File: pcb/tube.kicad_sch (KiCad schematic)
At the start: 79 parts, among them J1 Screw_Terminal_01x02, J10 LED_[5..8], J11 LED_[1..4], J2 Screw_Terminal_01x02, J3 Screw_Terminal_01x02, J4 Conn_01x04_Pin, J5 Conn_01x08_Pin, J6 Conn_01x05_Pin, U1 INA226, U10 74LS32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

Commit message: PCB: Use 0805
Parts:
- C1, C2, C3, C4, C5, C6, C7, C8: footprint Capacitor_SMD:C_0603_1608Metric -> Capacitor_SMD:C_0805_2012Metric
- R10, R11, R12, R13, R14, R15, R16, R17, R18, R19, R20, R21, R22, R23, R4, R5, R6, R7, R8, R9: footprint Resistor_SMD:R_0603_1608Metric -> Resistor_SMD:R_0805_2012Metric
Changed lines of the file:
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@@
       (effects (font (size 1.27 1.27)) (justify bottom))
     )
-    (property "Footprint" "Resistor_SMD:R_0603_1608Metric" (at 240.03 187.452 90)
+    (property "Footprint" "Resistor_SMD:R_0805_2012Metric" (at 240.03 187.452 90)
       (effects (font (size 1.27 1.27)) hide)
     )
@@
       (effects (font (size 1.27 1.27)) (justify right))
     )
-    (property "Footprint" "Resistor_SMD:R_0603_1608Metric" (at 61.468 101.6 90)
+    (property "Footprint" "Resistor_SMD:R_0805_2012Metric" (at 61.468 101.6 90)
       (effects (font (size 1.27 1.27)) hide)
     )
@@
       (effects (font (size 1.27 1.27)) (justify left))
     )
-    (property "Footprint" "Resistor_SMD:R_0603_1608Metric" (at 111.76 128.778 90)
+    (property "Footprint" "Resistor_SMD:R_0805_2012Metric" (at 111.76 128.778 90)
       (effects (font (size 1.27 1.27)) hide)
     )
@@
       (effects (font (size 1.27 1.27)) (justify left))
     )
-    (property "Footprint" "Resistor_SMD:R_0603_1608Metric" (at 199.898 198.12 90)
+    (property "Footprint" "Resistor_SMD:R_0805_2012Metric" (at 199.898 198.12 90)
       (effects (font (size 1.27 1.27)) hide)
     )
@@
       (effects (font (size 1.27 1.27)))
     )
-    (property "Footprint" "Capacitor_SMD:C_0603_1608Metric" (at 123.19 21.8948 0)
+    (property "Footprint" "Capacitor_SMD:C_0805_2012Metric" (at 123.19 21.8948 0)
       (effects (font (size 1.27 1.27)) hide)
     )
@@
       (effects (font (size 1.27 1.27)))
     )
-    (property "Footprint" "Capacitor_SMD:C_0603_1608Metric" (at 37.7952 242.57 0)
+    (property "Footprint" "Capacitor_SMD:C_0805_2012Metric" (at 37.7952 242.57 0)
       (effects (font (size 1.27 1.27)) hide)
     )
@@
       (effects (font (size 1.27 1.27)) (justify left))
     )
-    (property "Footprint" "Resistor_SMD:R_0603_1608Metric" (at 185.928 46.99 90)
+    (property "Footprint" "Resistor_SMD:R_0805_2012Metric" (at 185.928 46.99 90)
       (effects (font (size 1.27 1.27)) hide)
     )
@@
       (effects (font (size 1.27 1.27)))
     )
-    (property "Footprint" "Capacitor_SMD:C_0603_1608Metric" (at 124.46 159.7152 0)
+    (property "Footprint" "Capacitor_SMD:C_0805_2012Metric" (at 124.46 159.7152 0)
       (effects (font (size 1.27 1.27)) hide)
     )
@@
       (effects (font (size 1.27 1.27)) (justify left))
     )
-    (property "Footprint" "Resistor_SMD:R_0603_1608Metric" (at 111.76 131.318 90)
+    (property "Footprint" "Resistor_SMD:R_0805_2012Metric" (at 111.76 131.318 90)
       (effects (font (size 1.27 1.27)) hide)
     )
@@
       (effects (font (size 1.27 1.27)))
     )
-    (property "Footprint" "Capacitor_SMD:C_0603_1608Metric" (at 36.83 21.8948 0)
+    (property "Footprint" "Capacitor_SMD:C_0805_2012Metric" (at 36.83 21.8948 0)
       (effects (font (size 1.27 1.27)) hide)
     )
@@
       (effects (font (size 1.27 1.27)) (justify right))
     )
-    (property "Footprint" "Resistor_SMD:R_0603_1608Metric" (at 282.448 119.38 90)
+    (property "Footprint" "Resistor_SMD:R_0805_2012Metric" (at 282.448 119.38 90)
       (effects (font (size 1.27 1.27)) hide)
     )
@@
       (effects (font (size 1.27 1.27)) (justify left))
     )
-    (property "Footprint" "Resistor_SMD:R_0603_1608Metric" (at 111.76 138.938 90)
+    (property "Footprint" "Resistor_SMD:R_0805_2012Metric" (at 111.76 138.938 90)
       (effects (font (size 1.27 1.27)) hide)
     )
@@
       (effects (font (size 1.27 1.27)) (justify left))
     )
-    (property "Footprint" "Resistor_SMD:R_0603_1608Metric" (at 111.76 121.158 90)
+    (property "Footprint" "Resistor_SMD:R_0805_2012Metric" (at 111.76 121.158 90)
       (effects (font (size 1.27 1.27)) hide)
     )
@@
       (effects (font (size 1.27 1.27)))
     )
-    (property "Footprint" "Capacitor_SMD:C_0603_1608Metric" (at 80.01 21.8948 0)
+    (property "Footprint" "Capacitor_SMD:C_0805_2012Metric" (at 80.01 21.8948 0)
       (effects (font (size 1.27 1.27)) hide)
     )
@@
       (effects (font (size 1.27 1.27)) (justify left))
     )
-    (property "Footprint" "Resistor_SMD:R_0603_1608Metric" (at 111.76 123.698 90)
+    (property "Footprint" "Resistor_SMD:R_0805_2012Metric" (at 111.76 123.698 90)
       (effects (font (size 1.27 1.27)) hide)
     )
@@
       (effects (font (size 1.27 1.27)))
     )
-    (property "Footprint" "Capacitor_SMD:C_0603_1608Metric" (at 26.3652 242.57 0)
+    (property "Footprint" "Capacitor_SMD:C_0805_2012Metric" (at 26.3652 242.57 0)
       (effects (font (size 1.27 1.27)) hide)
     )
@@
       (effects (font (size 1.27 1.27)) (justify bottom))
     )
-    (property "Footprint" "Resistor_SMD:R_0603_1608Metric" (at 220.98 176.022 90)
+    (property "Footprint" "Resistor_SMD:R_0805_2012Metric" (at 220.98 176.022 90)
       (effects (font (size 1.27 1.27)) hide)
     )
@@
       (effects (font (size 1.27 1.27)) (justify right))
     )
-    (property "Footprint" "Resistor_SMD:R_0603_1608Metric" (at 52.578 101.6 90)
+    (property "Footprint" "Resistor_SMD:R_0805_2012Metric" (at 52.578 101.6 90)
       (effects (font (size 1.27 1.27)) hide)
     )
@@
       (effects (font (size 1.27 1.27)) (justify left))
     )
-    (property "Footprint" "Resistor_SMD:R_0603_1608Metric" (at 111.76 133.858 90)
+    (property "Footprint" "Resistor_SMD:R_0805_2012Metric" (at 111.76 133.858 90)
       (effects (font (size 1.27 1.27)) hide)
     )
@@
       (effects (font (size 1.27 1.27)) (justify right))
     )
-    (property "Footprint" "Resistor_SMD:R_0603_1608Metric" (at 43.688 101.6 90)
+    (property "Footprint" "Resistor_SMD:R_0805_2012Metric" (at 43.688 101.6 90)
       (effects (font (size 1.27 1.27)) hide)
     )
@@
       (effects (font (size 1.27 1.27)) (justify left))
     )
-    (property "Footprint" "Resistor_SMD:R_0603_1608Metric" (at 111.76 136.398 90)
+    (property "Footprint" "Resistor_SMD:R_0805_2012Metric" (at 111.76 136.398 90)
       (effects (font (size 1.27 1.27)) hide)
     )
@@
       (effects (font (size 1.27 1.27)) (justify bottom))
     )
-    (property "Footprint" "Resistor_SMD:R_0603_1608Metric" (at 214.63 187.452 90)
+    (property "Footprint" "Resistor_SMD:R_0805_2012Metric" (at 214.63 187.452 90)
       (effects (font (size 1.27 1.27)) hide)
     )
@@
       (effects (font (size 1.27 1.27)) (justify bottom))
     )
-    (property "Footprint" "Resistor_SMD:R_0603_1608Metric" (at 234.95 176.022 90)
+    (property "Footprint" "Resistor_SMD:R_0805_2012Metric" (at 234.95 176.022 90)
       (effects (font (size 1.27 1.27)) hide)
     )
@@
       (effects (font (size 1.27 1.27)))
     )
-    (property "Footprint" "Capacitor_SMD:C_0603_1608Metric" (at 290.5252 64.77 0)
+    (property "Footprint" "Capacitor_SMD:C_0805_2012Metric" (at 290.5252 64.77 0)
       (effects (font (size 1.27 1.27)) hide)
     )
@@
       (effects (font (size 1.27 1.27)))
     )
-    (property "Footprint" "Capacitor_SMD:C_0603_1608Metric" (at 277.8252 64.77 0)
+    (property "Footprint" "Capacitor_SMD:C_0805_2012Metric" (at 277.8252 64.77 0)
       (effects (font (size 1.27 1.27)) hide)
     )
@@
       (effects (font (size 1.27 1.27)) (justify left))
     )
-    (property "Footprint" "Resistor_SMD:R_0603_1608Metric" (at 174.498 46.99 90)
+    (property "Footprint" "Resistor_SMD:R_0805_2012Metric" (at 174.498 46.99 90)
       (effects (font (size 1.27 1.27)) hide)
     )
@@
       (effects (font (size 1.27 1.27)) (justify left))
     )
-    (property "Footprint" "Resistor_SMD:R_0603_1608Metric" (at 111.76 126.238 90)
+    (property "Footprint" "Resistor_SMD:R_0805_2012Metric" (at 111.76 126.238 90)
       (effects (font (size 1.27 1.27)) hide)
     )
@@
       (effects (font (size 1.27 1.27)) (justify right))
     )
-    (property "Footprint" "Resistor_SMD:R_0603_1608Metric" (at 276.098 106.68 90)
+    (property "Footprint" "Resistor_SMD:R_0805_2012Metric" (at 276.098 106.68 90)
       (effects (font (size 1.27 1.27)) hide)
     )

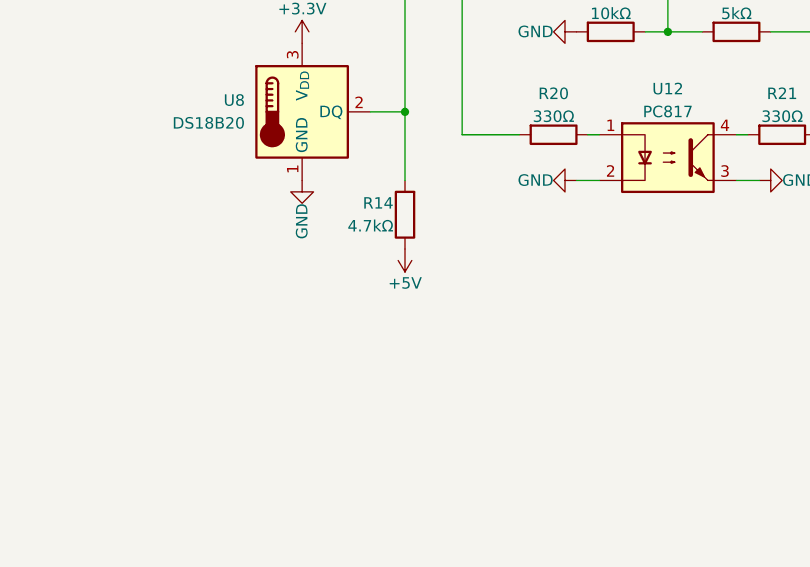
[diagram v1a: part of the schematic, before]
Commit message: PCB: Verify Pullups
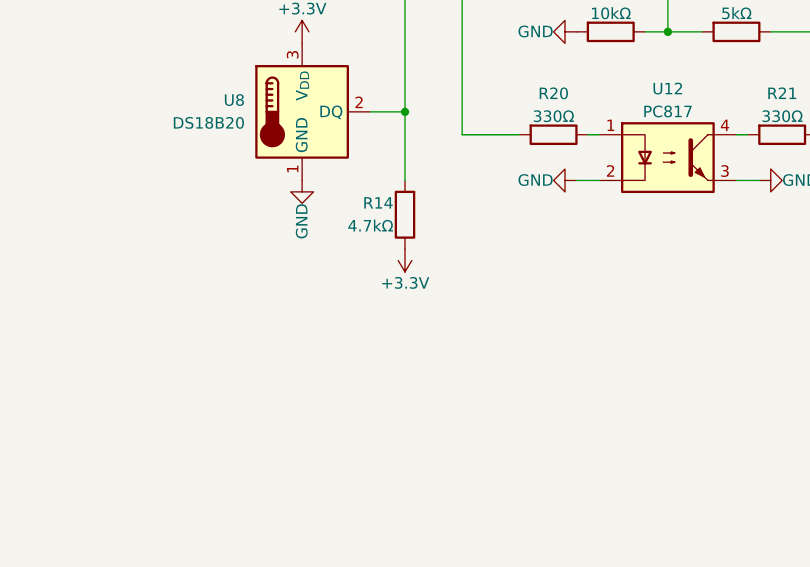
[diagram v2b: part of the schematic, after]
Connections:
- net +3.3V: now also R14.1
- net +5V: no longer R14.1
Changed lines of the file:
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@@
     )
   )
-  (symbol (lib_id "power:+5V") (at 198.12 201.93 180) (unit 1)
-    (in_bom yes) (on_board yes) (dnp no)
-    (property "Reference" "#PWR040" (at 198.12 198.12 0)
-      (effects (font (size 1.27 1.27)) hide)
-    )
-    (property "Value" "+5V" (at 198.12 205.74 0)
-      (effects (font (size 1.27 1.27)))
-    )
-    (property "Footprint" "" (at 198.12 201.93 0)
-      (effects (font (size 1.27 1.27)) hide)
-    )
-    (property "Datasheet" "" (at 198.12 201.93 0)
-      (effects (font (size 1.27 1.27)) hide)
-    )
-    (pin "1")
-    (instances
-      (project "tube"
-        (path "/17a681e7-f555-4501-b0f6-333651e2bfd6"
-          (reference "#PWR040") (unit 1)
-        )
-      )
-    )
-  )
   (symbol (lib_id "Connector:RJ45_Shielded") (at 67.31 173.99 0) (unit 1)
     (in_bom yes) (on_board yes) (dnp no)
@@
         )
       )
+    )
+  )
+  (symbol (lib_id "power:+3.3V") (at 198.12 201.93 180) (unit 1)
+    (in_bom yes) (on_board yes) (dnp no)
+    (property "Reference" "#PWR040" (at 198.12 198.12 0)
+      (effects (font (size 1.27 1.27)) hide)
+    )
+    (property "Value" "+3.3V" (at 198.12 205.74 0)
+      (effects (font (size 1.27 1.27)))
+    )
+    (property "Footprint" "" (at 198.12 201.93 0)
+      (effects (font (size 1.27 1.27)) hide)
+    )
+    (property "Datasheet" "" (at 198.12 201.93 0)
+      (effects (font (size 1.27 1.27)) hide)
+    )
+    (pin "1")
+    (instances
+      (project "tube"
+        (path "/17a681e7-f555-4501-b0f6-333651e2bfd6"
+          (reference "#PWR040") (unit 1)
+        )
+      )

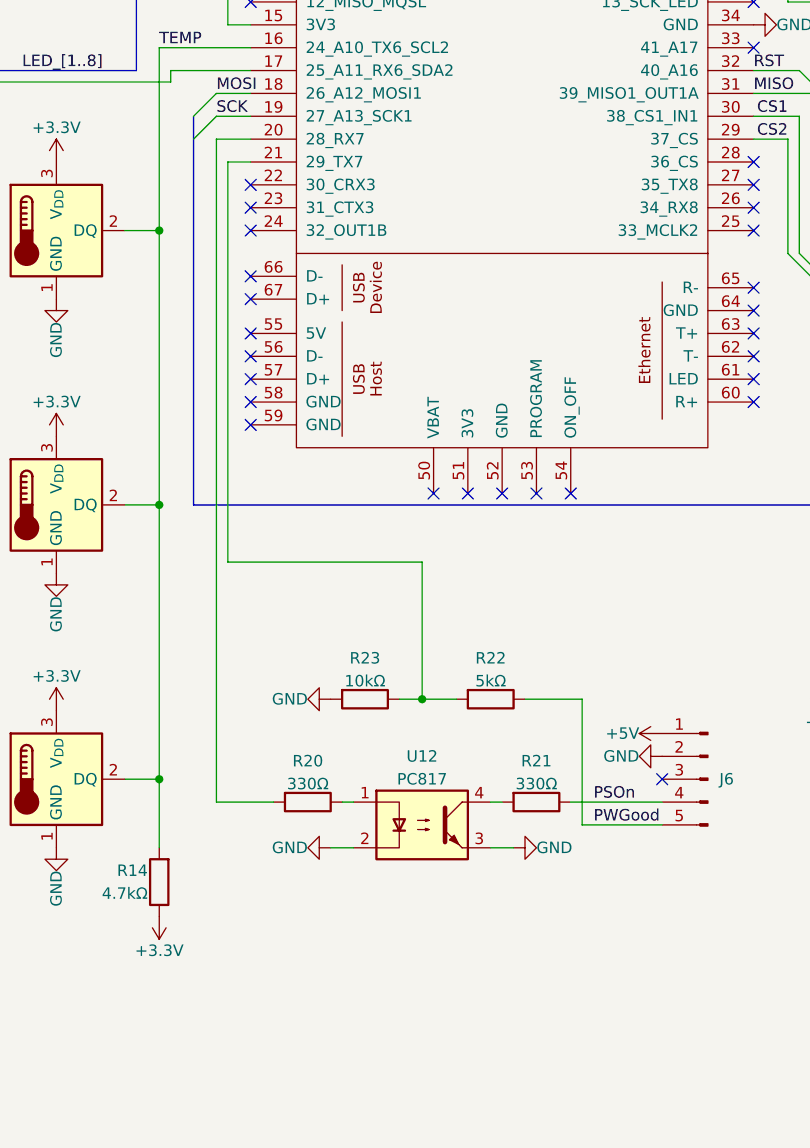
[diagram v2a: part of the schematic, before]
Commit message: PCB: Add Optocoppler For PWGood
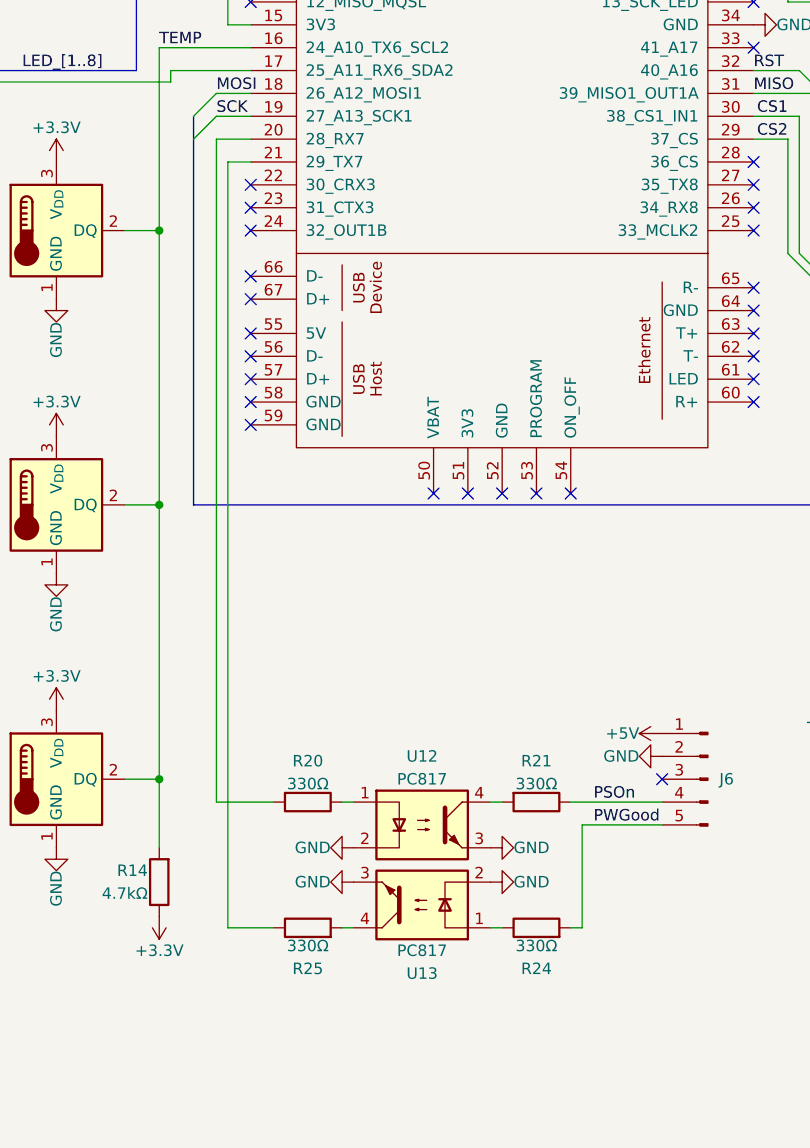
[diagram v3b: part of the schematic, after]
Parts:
- removed R22: 5kΩ, Resistor_SMD:R_0805_2012Metric, symbol Device:R
- removed R23: 10kΩ, Resistor_SMD:R_0805_2012Metric, symbol Device:R
- added R24, R25: 330Ω, Resistor_SMD:R_0805_2012Metric, symbol Device:R
- added U13: PC817, Package_DIP:DIP-4_W7.62mm, symbol Isolator:PC817
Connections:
- net GND: now also U13.2, U13.3
- net PWGood: now also R24.2
- net at U4.21 (29_TX7): now also R25.1
- new net: R25.2, U13.4
- new net: R24.1, U13.1

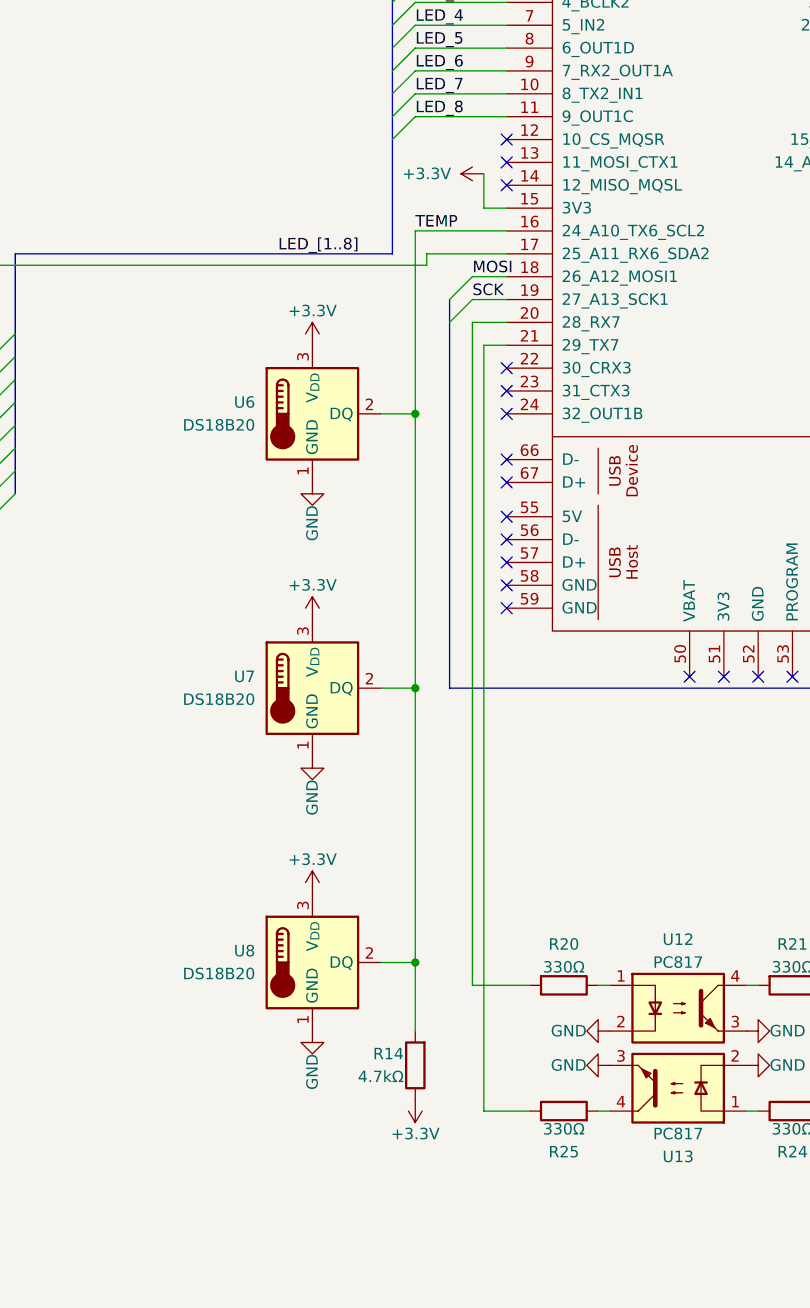
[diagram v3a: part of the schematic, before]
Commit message: PCB: Improve Power Traces
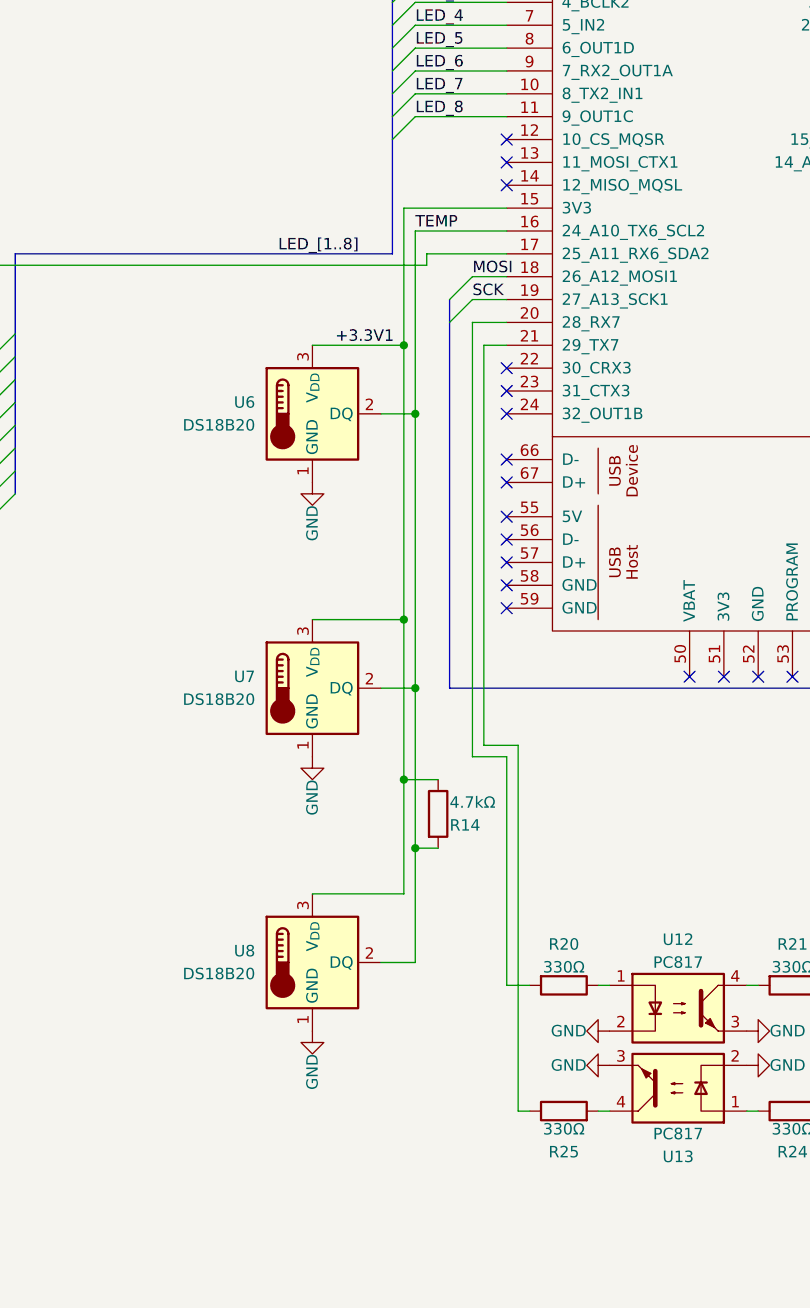
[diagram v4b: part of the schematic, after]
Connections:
- net +3.3V: no longer R14.1, U4.15 (3V3), U6.3 (V_{DD}), U7.3 (V_{DD}), U8.3 (V_{DD})
- new net +3.3V1: R14.1, U4.15 (3V3), U6.3 (V_{DD}), U7.3 (V_{DD}), U8.3 (V_{DD})
